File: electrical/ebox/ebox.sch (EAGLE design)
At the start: 12 parts, among them IC1 MAX3221CUE, U1 AT32UC3C1512/1256/1128, X1 22-23-2031, X2 22-23-2031, X3 C-GRID-07-70543, X4 22-23-2021, X5 C-GRID-07-70543, X6 C-GRID-07-70543, X7 C-GRID-07-70543, X8 C-GRID-07-70543, X9 C-GRID-07-70543

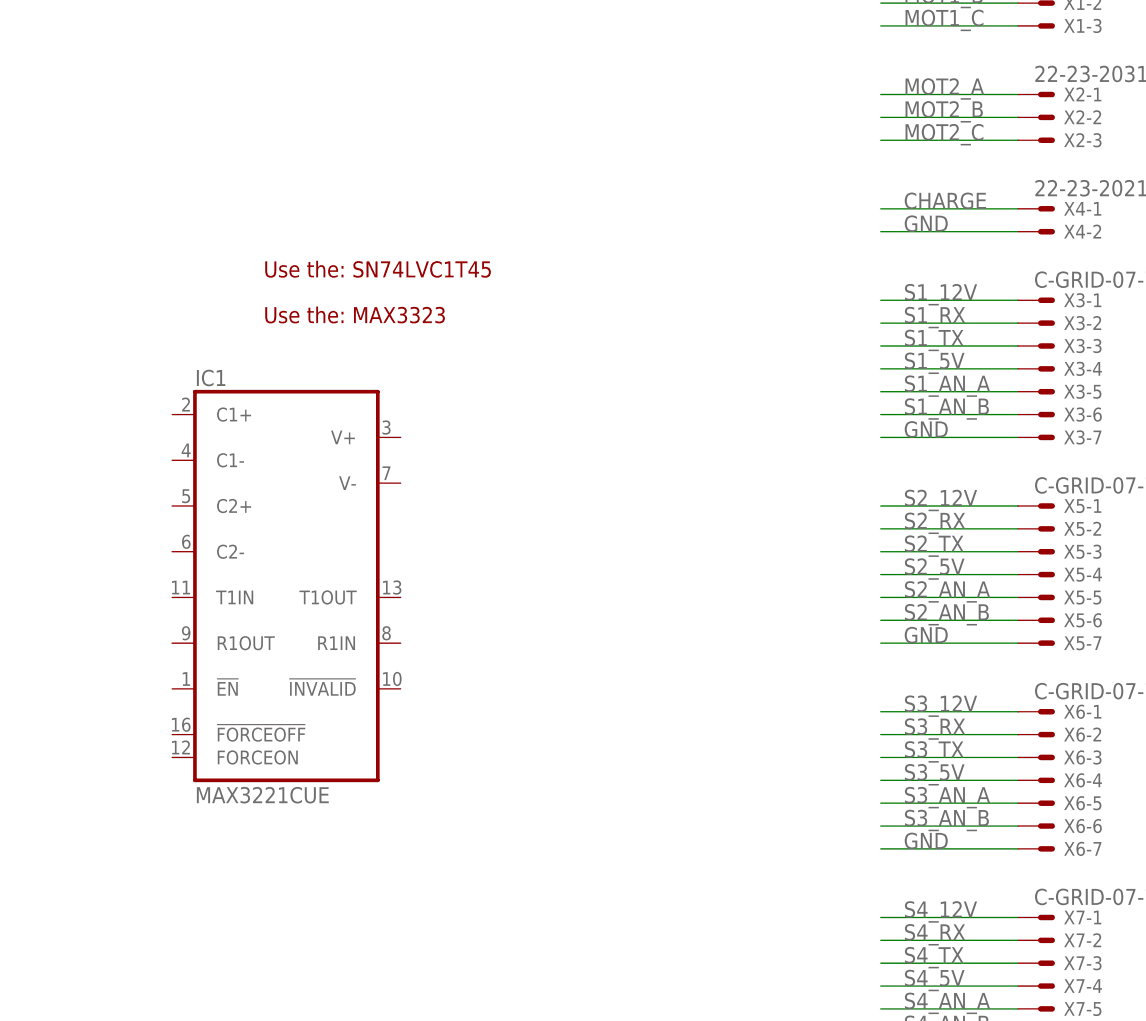
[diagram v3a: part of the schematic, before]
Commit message: Made notes for how to do all the IO.
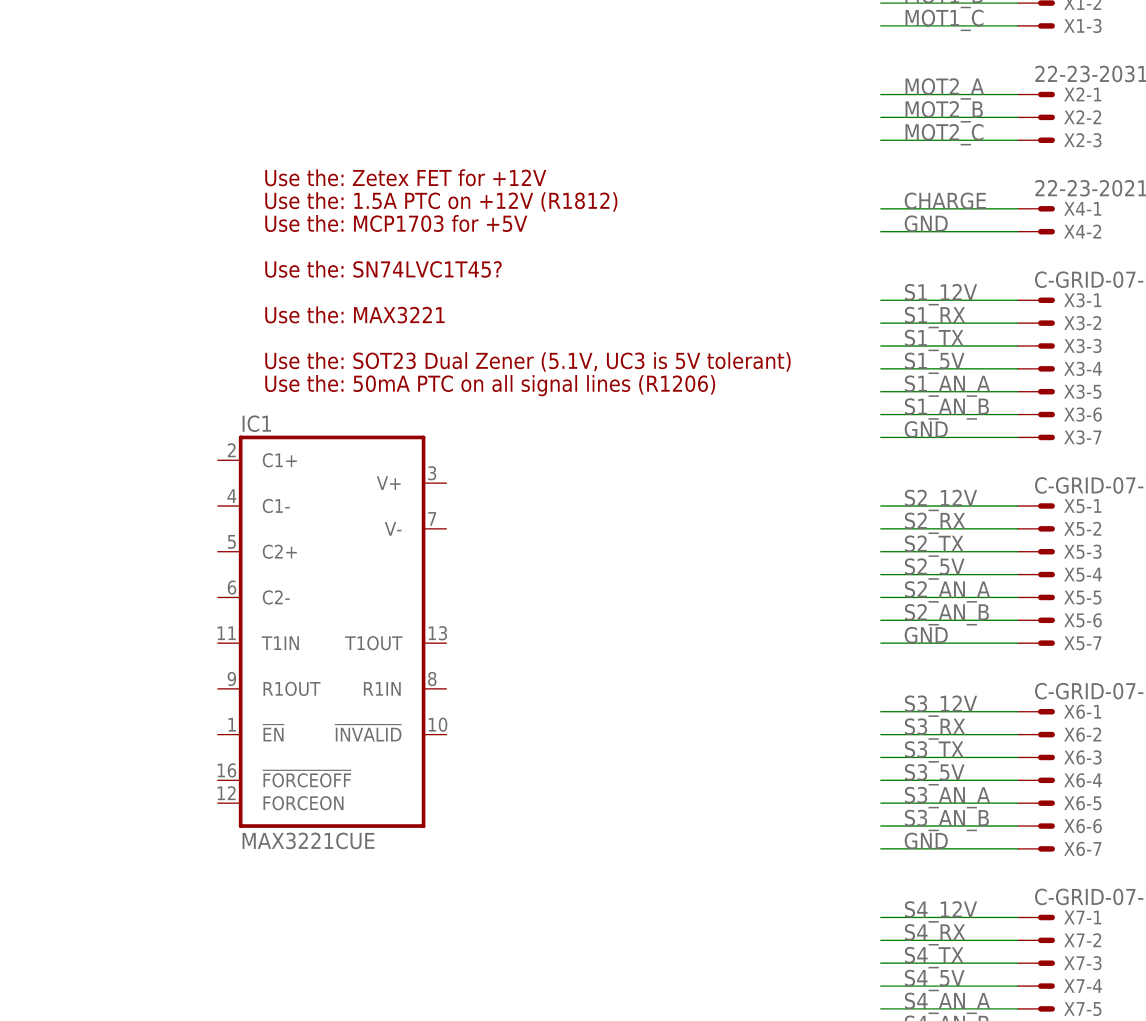
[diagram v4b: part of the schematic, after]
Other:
- note added: "Use the: 1.5A PTC on +12V (R1812)"
- note added: "Use the: 50mA PTC on all signal lines (R1206)"
- note added: "Use the: MAX3221"
- note added: "Use the: MCP1703 for +5V"
- note added: "Use the: SN74LVC1T45?"
- note added: "Use the: SOT23 Dual Zener (5.1V, UC3 is 5V tolerant)"
- note added: "Use the: Zetex FET for +12V"
- note removed: "Use the: MAX3323"
- note removed: "Use the: SN74LVC1T45"
- moved on the sheet: IC1
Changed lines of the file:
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@@
 <text x="355.6" y="246.38" size="1.778" layer="94">TODO: Replace with multi-con-X</text>
 <text x="355.6" y="243.84" size="1.778" layer="94">TODO: Replace with mini-con-x</text>
-<text x="281.94" y="205.74" size="1.778" layer="94">Use the: SN74LVC1T45</text>
-<text x="281.94" y="200.66" size="1.778" layer="94">Use the: MAX3323</text>
+<text x="281.94" y="205.74" size="1.778" layer="94">Use the: SN74LVC1T45?</text>
+<text x="281.94" y="200.66" size="1.778" layer="94">Use the: MAX3221</text>
+<text x="281.94" y="195.58" size="1.778" layer="94">Use the: SOT23 Dual Zener (5.1V, UC3 is 5V tolerant)</text>
+<text x="281.94" y="193.04" size="1.778" layer="94">Use the: 50mA PTC on all signal lines (R1206)</text>
+<text x="281.94" y="210.82" size="1.778" layer="94">Use the: MCP1703 for +5V</text>
+<text x="281.94" y="215.9" size="1.778" layer="94">Use the: Zetex FET for +12V</text>
+<text x="281.94" y="213.36" size="1.778" layer="94">Use the: 1.5A PTC on +12V (R1812)</text>
 </plain>
 <instances>
@@
 <instance part="U$1" gate="G$1" x="104.14" y="238.76"/>
 <instance part="U1" gate="NAME" x="147.32" y="132.08"/>
-<instance part="IC1" gate="G$1" x="284.48" y="175.26"/>
+<instance part="IC1" gate="G$1" x="289.56" y="170.18"/>
 </instances>
 <busses>

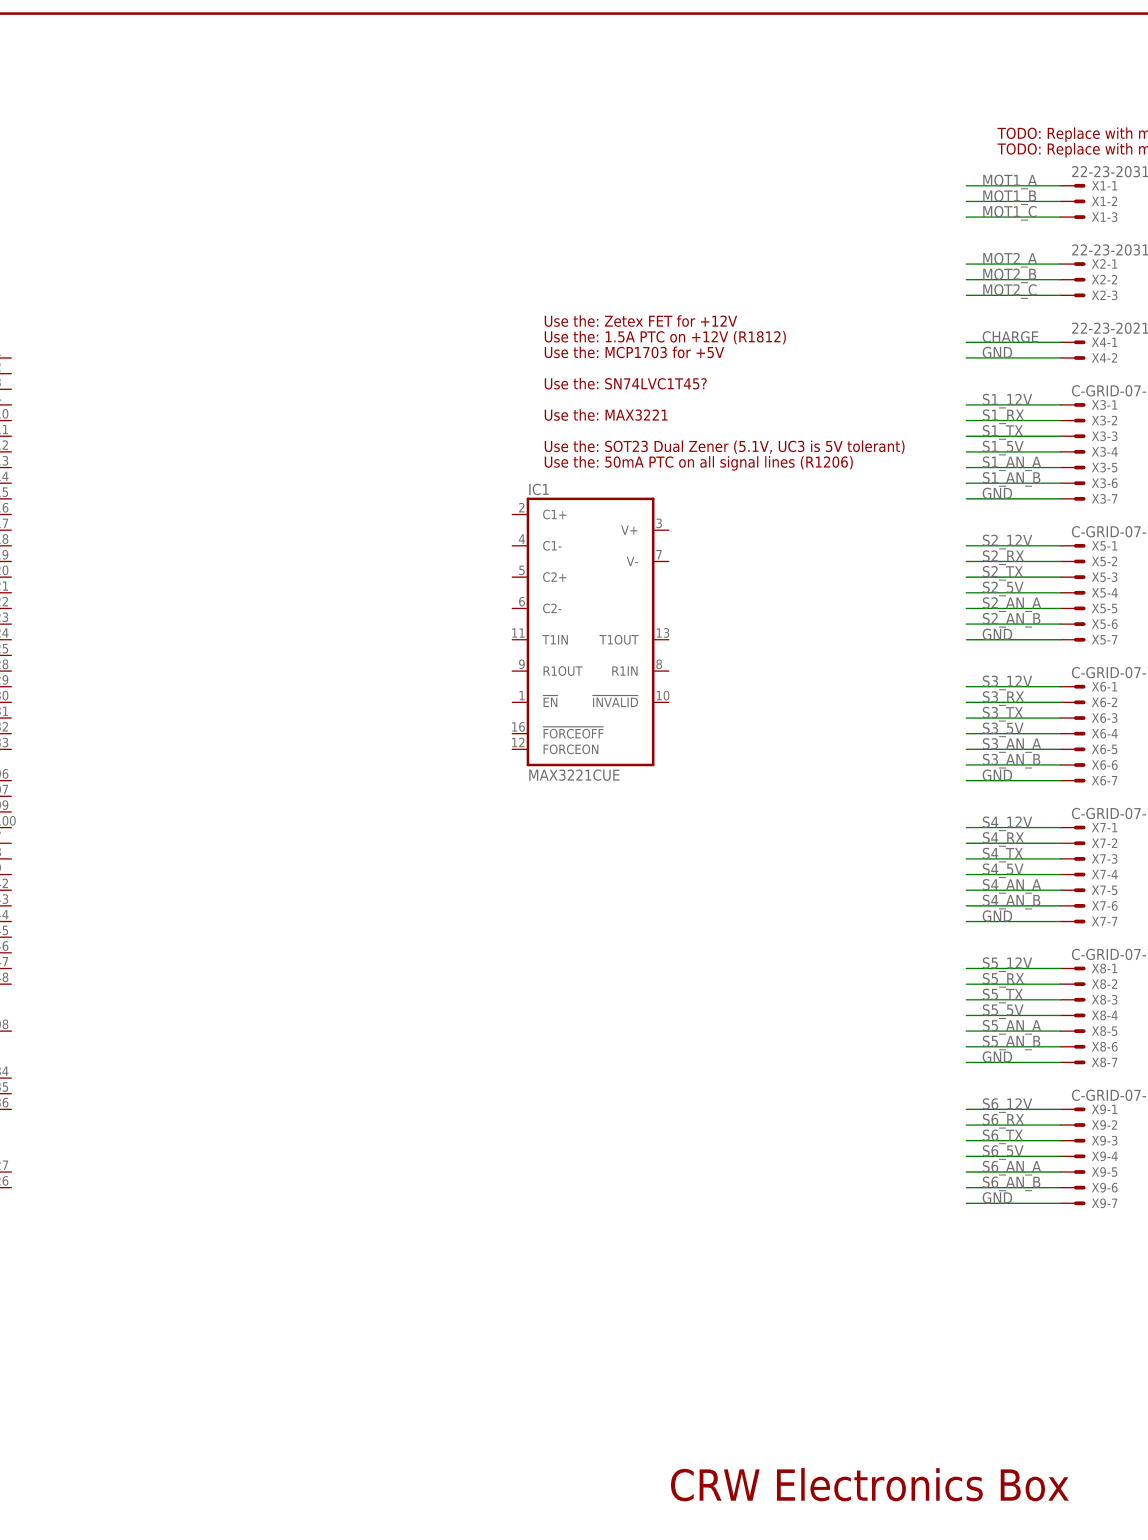
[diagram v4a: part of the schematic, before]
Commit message: Laid out RS232 component for omni-sensor.
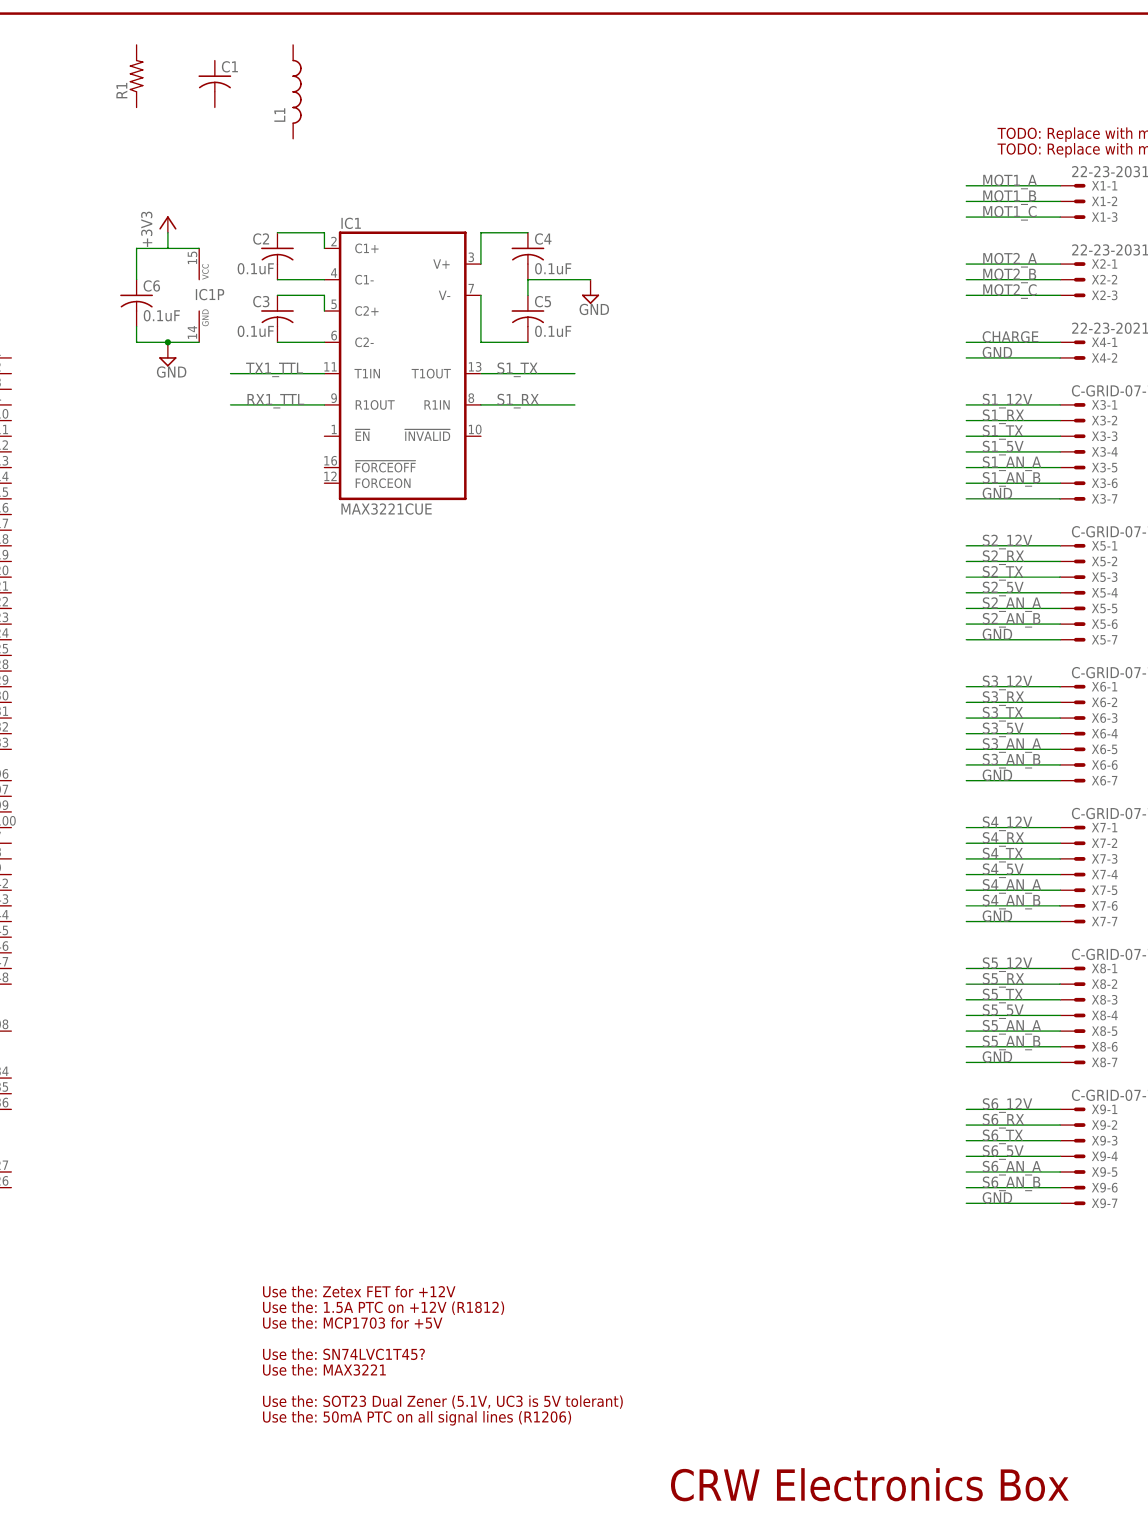
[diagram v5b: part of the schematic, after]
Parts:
- added C1: (no value), rcl:C-USC0805
- added C2, C3, C4, C5, C6: 0.1uF, rcl:C-USC0805
- added L1: (no value), rcl:L-USL2012C
- added R1: (no value), rcl:R-US_R0805
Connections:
- new net +3V3: C6.1, IC1P.VCC
- new net N$1: C2.2, IC1G$1.C1-
- new net N$10: C4.1, IC1G$1.V+
- new net N$11: C5.2, IC1G$1.V-
- new net N$2: C2.1, IC1G$1.C1+
- new net N$3: C3.1, IC1G$1.C2+
- new net N$4: C3.2, IC1G$1.C2-
- new net RX1_TTL: IC1G$1.R1OUT
- new net TX1_TTL: IC1G$1.T1IN
- net GND: now also C4.2, C5.1, C6.2, IC1P.GND
- net S1_RX: now also IC1G$1.R1IN
- net S1_TX: now also IC1G$1.T1OUT
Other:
- moved on the sheet: IC1
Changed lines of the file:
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@@
 <setting verticaltext="up"/>
 </settings>
-<grid distance="0.1" unitdist="inch" unit="inch" style="lines" multiple="1" display="no" altdistance="0.01" altunitdist="inch" altunit="inch"/>
+<grid distance="0.1" unitdist="inch" unit="inch" style="lines" multiple="1" display="yes" altdistance="0.01" altunitdist="inch" altunit="inch"/>
 <layers>
 <layer number="1" name="Top" color="4" fill="1" visible="no" active="no"/>
@@
 <part name="U1" library="atmel-avr32-michel" deviceset="AT32UC3C1512/1256/1128" device=""/>
 <part name="IC1" library="maxim" deviceset="MAX3221*" device="UE" technology="C"/>
+<part name="R1" library="rcl" deviceset="R-US_" device="R0805"/>
+<part name="C1" library="rcl" deviceset="C-US" device="C0805"/>
+<part name="L1" library="rcl" deviceset="L-US" device="L2012C"/>
+<part name="C2" library="rcl" deviceset="C-US" device="C0805" value="0.1uF"/>
+<part name="C3" library="rcl" deviceset="C-US" device="C0805" value="0.1uF"/>
+<part name="C4" library="rcl" deviceset="C-US" device="C0805" value="0.1uF"/>
+<part name="C5" library="rcl" deviceset="C-US" device="C0805" value="0.1uF"/>
+<part name="SUPPLY1" library="supply2" deviceset="GND" device=""/>
+<part name="C6" library="rcl" deviceset="C-US" device="C0805" value="0.1uF"/>
+<part name="SUPPLY2" library="supply2" deviceset="GND" device=""/>
+<part name="+3V1" library="supply1" deviceset="+3V3" device=""/>
 </parts>
 <sheets>
@@
 <text x="355.6" y="246.38" size="1.778" layer="94">TODO: Replace with multi-con-X</text>
 <text x="355.6" y="243.84" size="1.778" layer="94">TODO: Replace with mini-con-x</text>
-<text x="281.94" y="205.74" size="1.778" layer="94">Use the: SN74LVC1T45?</text>
-<text x="281.94" y="200.66" size="1.778" layer="94">Use the: MAX3221</text>
-<text x="281.94" y="195.58" size="1.778" layer="94">Use the: SOT23 Dual Zener (5.1V, UC3 is 5V tolerant)</text>
-<text x="281.94" y="193.04" size="1.778" layer="94">Use the: 50mA PTC on all signal lines (R1206)</text>
-<text x="281.94" y="210.82" size="1.778" layer="94">Use the: MCP1703 for +5V</text>
-<text x="281.94" y="215.9" size="1.778" layer="94">Use the: Zetex FET for +12V</text>
-<text x="281.94" y="213.36" size="1.778" layer="94">Use the: 1.5A PTC on +12V (R1812)</text>
+<text x="236.22" y="48.26" size="1.778" layer="94">Use the: SN74LVC1T45?</text>
+<text x="236.22" y="45.72" size="1.778" layer="94">Use the: MAX3221</text>
+<text x="236.22" y="40.64" size="1.778" layer="94">Use the: SOT23 Dual Zener (5.1V, UC3 is 5V tolerant)</text>
+<text x="236.22" y="38.1" size="1.778" layer="94">Use the: 50mA PTC on all signal lines (R1206)</text>
+<text x="236.22" y="53.34" size="1.778" layer="94">Use the: MCP1703 for +5V</text>
+<text x="236.22" y="58.42" size="1.778" layer="94">Use the: Zetex FET for +12V</text>
+<text x="236.22" y="55.88" size="1.778" layer="94">Use the: 1.5A PTC on +12V (R1812)</text>
 </plain>
 <instances>
@@
 <instance part="U$1" gate="G$1" x="104.14" y="238.76"/>
 <instance part="U1" gate="NAME" x="147.32" y="132.08"/>
-<instance part="IC1" gate="G$1" x="289.56" y="170.18"/>
+<instance part="IC1" gate="G$1" x="259.08" y="213.36"/>
+<instance part="R1" gate="G$1" x="215.9" y="256.54" rot="R90"/>
+<instance part="C1" gate="G$1" x="228.6" y="256.54"/>
+<instance part="L1" gate="G$1" x="241.3" y="254"/>
+<instance part="C2" gate="G$1" x="238.76" y="228.6" smashed="yes">
+<attribute name="NAME" x="234.696" y="229.235" size="1.778" layer="95"/>
+<attribute name="VALUE" x="232.156" y="224.409" size="1.778" layer="96"/>
+</instance>
+<instance part="C3" gate="G$1" x="238.76" y="218.44" smashed="yes">
+<attribute name="NAME" x="234.696" y="219.075" size="1.778" layer="95"/>
+<attribute name="VALUE" x="232.156" y="214.249" size="1.778" layer="96"/>
+</instance>
+<instance part="C4" gate="G$1" x="279.4" y="228.6"/>
+<instance part="C5" gate="G$1" x="279.4" y="218.44"/>
+<instance part="SUPPLY1" gate="GND" x="289.56" y="220.98"/>
+<instance part="IC1" gate="P" x="226.06" y="220.98"/>
+<instance part="C6" gate="G$1" x="215.9" y="220.98"/>
+<instance part="SUPPLY2" gate="GND" x="220.98" y="210.82"/>
+<instance part="+3V1" gate="G$1" x="220.98" y="233.68"/>
 </instances>
 <busses>
@@
 <label x="353.06" y="73.66" size="1.778" layer="95"/>
 </segment>
+<segment>
+<pinref part="C4" gate="G$1" pin="2"/>
+<pinref part="C5" gate="G$1" pin="1"/>
+<wire x1="279.4" y1="220.98" x2="279.4" y2="223.52" width="0.1524" layer="91"/>
+<wire x1="279.4" y1="223.52" x2="289.56" y2="223.52" width="0.1524" layer="91"/>
+<pinref part="SUPPLY1" gate="GND" pin="GND"/>
+</segment>
+<segment>
+<pinref part="C6" gate="G$1" pin="2"/>
+<wire x1="215.9" y1="215.9" x2="215.9" y2="213.36" width="0.1524" layer="91"/>
+<pinref part="IC1" gate="P" pin="GND"/>
+<wire x1="215.9" y1="213.36" x2="220.98" y2="213.36" width="0.1524" layer="91"/>
+<pinref part="SUPPLY2" gate="GND" pin="GND"/>
+<wire x1="220.98" y1="213.36" x2="226.06" y2="213.36" width="0.1524" layer="91"/>
+<junction x="220.98" y="213.36"/>
+</segment>
 </net>
 <net name="S1_12V" class="0">
@@
 <label x="353.06" y="200.66" size="1.778" layer="95"/>
 </segment>
+<segment>
+<pinref part="IC1" gate="G$1" pin="R1IN"/>
+<wire x1="271.78" y1="203.2" x2="287.02" y2="203.2" width="0.1524" layer="91"/>
+<label x="274.32" y="203.2" size="1.778" layer="95"/>
+</segment>
 </net>
 <net name="S1_TX" class="0">
@@
 <label x="353.06" y="198.12" size="1.778" layer="95"/>
 </segment>
+<segment>
+<pinref part="IC1" gate="G$1" pin="T1OUT"/>
+<wire x1="271.78" y1="208.28" x2="287.02" y2="208.28" width="0.1524" layer="91"/>
+<label x="274.32" y="208.28" size="1.778" layer="95"/>
+</segment>
 </net>
 <net name="S1_5V" class="0">
@@
 </segment>
 </net>
+<net name="N$1" class="0">
+<segment>
+<pinref part="C2" gate="G$1" pin="2"/>
+<pinref part="IC1" gate="G$1" pin="C1-"/>
+<wire x1="238.76" y1="223.52" x2="246.38" y2="223.52" width="0.1524" layer="91"/>
+</segment>
+</net>
+<net name="N$2" class="0">
+<segment>
+<pinref part="C2" gate="G$1" pin="1"/>
+<wire x1="238.76" y1="231.14" x2="246.38" y2="231.14" width="0.1524" layer="91"/>
+<pinref part="IC1" gate="G$1" pin="C1+"/>
+<wire x1="246.38" y1="231.14" x2="246.38" y2="228.6" width="0.1524" layer="91"/>
+</segment>
+</net>
+<net name="N$4" class="0">
+<segment>
+<pinref part="C3" gate="G$1" pin="2"/>
+<wire x1="238.76" y1="213.36" x2="246.38" y2="213.36" width="0.1524" layer="91"/>
+<pinref part="IC1" gate="G$1" pin="C2-"/>
+</segment>
+</net>
+<net name="N$3" class="0">
+<segment>
+<pinref part="C3" gate="G$1" pin="1"/>
+<wire x1="238.76" y1="220.98" x2="246.38" y2="220.98" width="0.1524" layer="91"/>
+<pinref part="IC1" gate="G$1" pin="C2+"/>
+<wire x1="246.38" y1="220.98" x2="246.38" y2="218.44" width="0.1524" layer="91"/>
+</segment>
+</net>
+<net name="TX1_TTL" class="0">
+<segment>
+<pinref part="IC1" gate="G$1" pin="T1IN"/>
+<wire x1="246.38" y1="208.28" x2="231.14" y2="208.28" width="0.1524" layer="91"/>
+<label x="233.68" y="208.28" size="1.778" layer="95"/>
+</segment>
+</net>
+<net name="RX1_TTL" class="0">
+<segment>
+<pinref part="IC1" gate="G$1" pin="R1OUT"/>
+<wire x1="246.38" y1="203.2" x2="231.14" y2="203.2" width="0.1524" layer="91"/>
+<label x="233.68" y="203.2" size="1.778" layer="95"/>
+</segment>
+</net>
+<net name="N$10" class="0">
+<segment>
+<pinref part="IC1" gate="G$1" pin="V+"/>
+<wire x1="271.78" y1="226.06" x2="271.78" y2="231.14" width="0.1524" layer="91"/>
+<pinref part="C4" gate="G$1" pin="1"/>
+<wire x1="271.78" y1="231.14" x2="279.4" y2="231.14" width="0.1524" layer="91"/>
+</segment>
+</net>
+<net name="N$11" class="0">
+<segment>
+<pinref part="IC1" gate="G$1" pin="V-"/>
+<wire x1="271.78" y1="220.98" x2="271.78" y2="213.36" width="0.1524" layer="91"/>
+<wire x1="271.78" y1="213.36" x2="279.4" y2="213.36" width="0.1524" layer="91"/>
+<pinref part="C5" gate="G$1" pin="2"/>
+</segment>
+</net>
+<net name="+3V3" class="0">
+<segment>
+<pinref part="C6" gate="G$1" pin="1"/>
+<wire x1="215.9" y1="223.52" x2="215.9" y2="228.6" width="0.1524" layer="91"/>
+<pinref part="IC1" gate="P" pin="VCC"/>
+<wire x1="215.9" y1="228.6" x2="220.98" y2="228.6" width="0.1524" layer="91"/>
+<pinref part="+3V1" gate="G$1" pin="+3V3"/>
+<wire x1="220.98" y1="228.6" x2="226.06" y2="228.6" width="0.1524" layer="91"/>
+<wire x1="220.98" y1="228.6" x2="220.98" y2="231.14" width="0.1524" layer="91"/>
+</segment>
+</net>
